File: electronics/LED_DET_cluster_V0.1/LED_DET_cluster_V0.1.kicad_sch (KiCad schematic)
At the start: 5 parts, among them J1 Conn_01x06, J2 Conn_01x06, U1 PPG_sensor_PD_4_LED

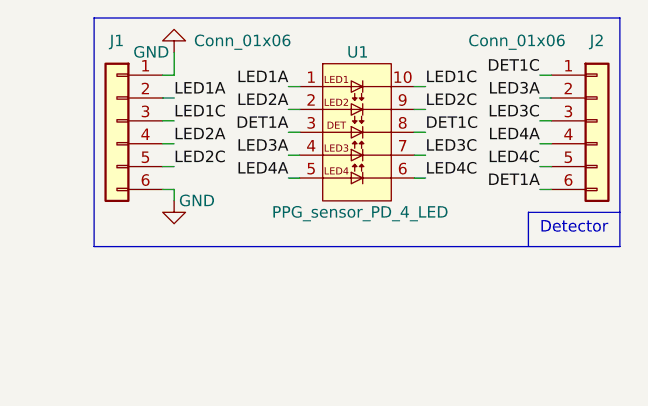
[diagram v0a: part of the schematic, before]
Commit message: completed LED detector cluster 0.1
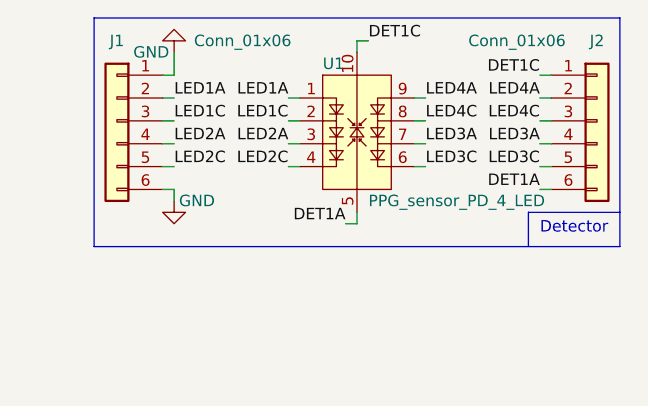
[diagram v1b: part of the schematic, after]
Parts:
- U1: footprint (none) -> SquantorOpto:PPG_sensor_4LED
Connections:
- net DET1A: now also U1.5; no longer U1.3
- net DET1C: now also U1.10; no longer U1.8
- net LED1C: now also U1.2; no longer U1.10
- net LED2A: now also U1.3; no longer U1.2
- net LED2C: now also U1.4; no longer U1.9
- net LED3A: now also J2.4 (Pin_4), U1.7; no longer J2.2 (Pin_2), U1.4
- net LED3C: now also J2.5 (Pin_5), U1.6; no longer J2.3 (Pin_3), U1.7
- net LED4A: now also J2.2 (Pin_2), U1.9; no longer J2.4 (Pin_4), U1.5
- net LED4C: now also J2.3 (Pin_3), U1.8; no longer J2.5 (Pin_5), U1.6

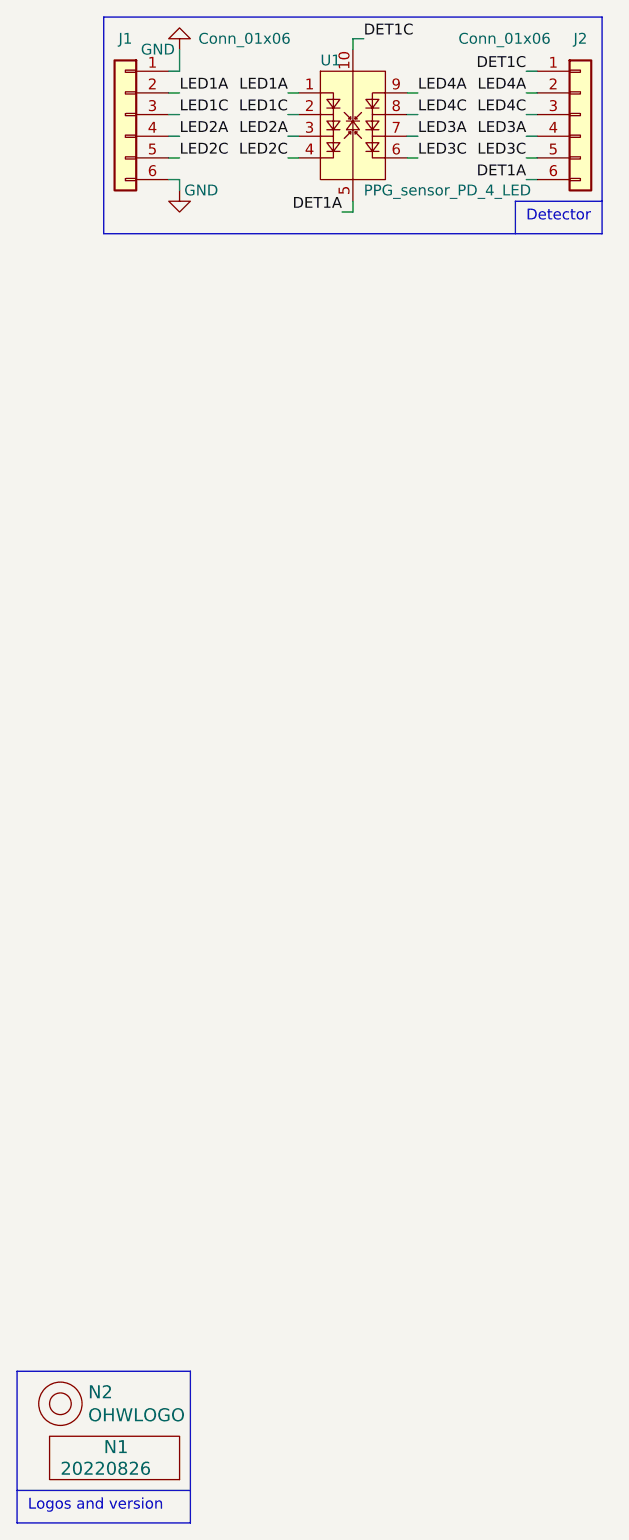
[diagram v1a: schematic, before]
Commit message: updated PPG LED detector cluster
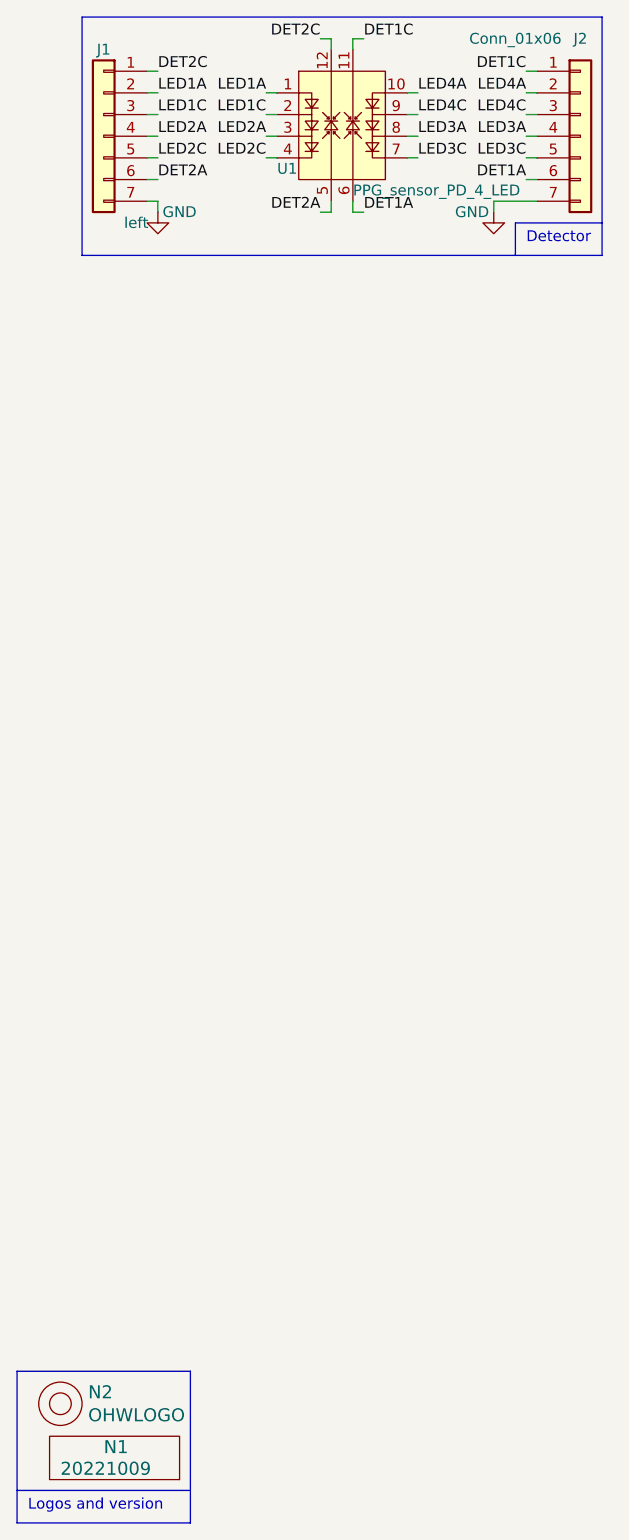
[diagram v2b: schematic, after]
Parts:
- J1: value Conn_01x06 -> left; footprint SquantorConnectors:Header-0254-1X06-H010 -> SquantorConnectors:Header-0254-1X07-H010; symbol Connector_Generic:Conn_01x06 -> Connector_Generic:Conn_01x07
- J2: footprint SquantorConnectors:Header-0254-1X06-H010 -> SquantorConnectors:Header-0254-1X07-H010; symbol Connector_Generic:Conn_01x06 -> Connector_Generic:Conn_01x07
- N1: value 20220826 -> 20221009
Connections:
- net DET1A: now also U1.6; no longer U1.5
- net DET1C: now also U1.11; no longer U1.10
- net GND: now also J1.7 (Pin_7), J2.7 (Pin_7); no longer J1.1 (Pin_1), J1.6 (Pin_6)
- net LED3A: now also U1.8; no longer U1.7
- net LED3C: now also U1.7; no longer U1.6
- net LED4A: now also U1.10; no longer U1.9
- net LED4C: now also U1.9; no longer U1.8
- new net DET2A: J1.6 (Pin_6), U1.5
- new net DET2C: J1.1 (Pin_1), U1.12
